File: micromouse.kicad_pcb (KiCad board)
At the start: 2 copper layers, 115.3 x 122.3 mm, 14 parts, among them J1 XT60-M, SW2 SW_Push, SW3 SW_SPDT_312, SW4 SW_Push, U1 BUCK, U2 STM32 Blackpill, U3 N20 encoder right, U4 N20 encoder left, U5 TB6612FNG, U6 VL53L0X left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

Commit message: pcb
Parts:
- SW2, SW4: footprint push button:push_button -> push button 1:SW_VS-1213-67-160GF
- moved U7 2.27 mm to (183.3, 50.1)
- moved SW4 1.72 mm to (129.1, 63.4)
- moved SW2 1.69 mm to (170.9, 63.3)
- moved U6 1.08 mm to (116.8, 67.8)
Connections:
- U5 pad 2: 5v -> 3.3v
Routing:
- net 3.3v: track 268.7 -> 324.7 mm
- net 5v: track 104.5 -> 83.3 mm
- net XSHUT 3: track 51.2 -> 53.9 mm
- net SCL: track 216.0 -> 218.2 mm
- net XSHUT 1: track 50.6 -> 51.9 mm
- net SDA: track 194.5 -> 193.7 mm
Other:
- board size 115.3 x 122.3 mm -> 115 x 122.4 mm

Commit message: pcb changes
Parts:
- added G***: LOGO, rnc:rnc3, F.Cu at (129.7, 49.1)
- added SW1: SW_SPST, power switch:battery_sw, F.Cu at (195.4, 131.8)
- moved U7 0.91 mm to (182.8, 49.4)
- moved U6 0.90 mm to (117.5, 67.2)
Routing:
- net 7.4vb: track 11.5 -> 38.3 mm
- net 7.4v: track 0.00 -> 15.0 mm
- net AIN1: track 45.7 -> 47.5 mm
- net XSHUT 1: track 51.9 -> 50.6 mm
- net BO2: track 30.1 -> 31.1 mm
- net XSHUT 3: track 53.9 -> 53.1 mm
- net AIN2: track 45.7 -> 46.5 mm
- net SDA: track 193.7 -> 193.1 mm
- net SCL: track 218.2 -> 218.8 mm
- added copper zone on B.Cu, net GND
- added copper zone on F.Cu, net GND
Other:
- outline, holes or cut-outs redrawn

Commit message: changes
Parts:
- moved U7 2.29 mm to (180.9, 48.1)
- moved U6 2.16 mm to (119.1, 65.8)
- moved U8 0.33 mm to (140.9, 44.2)
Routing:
- net SDA: track 193.1 -> 190.0 mm
- net XSHUT 3: track 53.1 -> 55.3 mm
- net GND: track 367.5 -> 366.2 mm
- net 3.3v: track 324.6 -> 323.3 mm
- net XSHUT 1: track 50.6 -> 51.3 mm

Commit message: final
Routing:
- net slide_SW: track 55.5 -> 86.6 mm, vias 1 -> 0
- net SCL: track 219.2 -> 189.6 mm
- net GND: track 366.2 -> 395.0 mm
- net XSHUT 3: track 55.3 -> 37.7 mm
- net STBY: track 88.6 -> 103.7 mm, vias 0 -> 1
- net 3.3v: track 323.3 -> 308.8 mm, vias 0 -> 1
- net XSHUT 1: track 51.3 -> 57.9 mm
- net BO1: track 67.9 -> 71.0 mm
- net XSHUT 2: track 54.5 -> 53.3 mm
- net AO1: track 24.8 -> 26.0 mm
- net push button: track 30.6 -> 31.5 mm
- net SDA: track 190.0 -> 189.3 mm
- net push button 1: track 57.9 -> 58.5 mm
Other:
- outline, holes or cut-outs redrawn

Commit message: hello world
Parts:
- removed G***: LOGO, rnc:rnc3
- removed U9: oled i2c, oled:oled
- ACC1: moved to B.Cu
- U6: value VL53L0X left -> VL6180X; footprint VL53L0X:VL53L0X -> VL6180X:VL6180X
- U7: value VL53L0X right -> VL6180X; footprint VL53L0X:VL53L0X -> VL6180X:VL6180X
- U8: value VL53L0X middle -> VL6180X; footprint VL53L0X:VL53L0X -> VL6180X:VL6180X
- moved SW2 279.7 mm to (-108.8, 65.7), turned to 0 degrees
- moved J1 263.0 mm to (-48.8, 53.1), turned to 90 degrees
- moved U2 257.7 mm to (-117.1, 100.6), turned to 0 degrees
- moved SW1 247.7 mm to (-49.3, 93.3), turned to -90 degrees
- moved SW3 235.7 mm to (405.8, 91.7)
- moved U1 230.4 mm to (-50.0, 77.0), turned to 180 degrees
- moved SW4 197.1 mm to (-68.0, 66.3), turned to 0 degrees
- moved U3 181.6 mm to (-12.2, 87.9)
- moved U4 146.6 mm to (-12.1, 58.9)
- moved U5 66.3 mm to (147.6, 73.4), turned to 90 degrees
- moved U6 54.0 mm to (171.5, 52.8), turned to -90 degrees
- moved U7 32.7 mm to (148.9, 55.0), turned to 0 degrees
- moved U8 18.1 mm to (124.1, 51.0), turned to 90 degrees
- moved ACC1 2.89 mm to (158.5, 71.9), turned to -90 degrees
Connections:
- U6 pad 1: 3.3v -> unconnected-(U6-GPIO1-Pad1)
- U6 pad 2: GND -> XSHUT 3
- U6 pad 5: unconnected-(U6-GPIO1-Pad5) -> 3.3v
- U6 pad 6: XSHUT 3 -> GND
- U7 pad 1: 3.3v -> unconnected-(U7-GPIO1-Pad1)
- U7 pad 2: GND -> XSHUT 1
- U7 pad 5: unconnected-(U7-GPIO1-Pad5) -> 3.3v
- U7 pad 6: XSHUT 1 -> GND
- U8 pad 1: 3.3v -> (no net)
- U8 pad 2: GND -> (no net)
- U8 pad 3: SCL -> (no net)
- U8 pad 4: SDA -> (no net)
- U8 pad 5: unconnected-(U8-GPIO1-Pad5) -> (no net)
- U8 pad 6: XSHUT 2 -> (no net)
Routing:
- net GND: track 395.0 -> 0.00 mm
- net 3.3v: track 308.8 -> 0.00 mm, vias 1 -> 0
- net SCL: track 189.6 -> 0.00 mm, vias 1 -> 0
- net SDA: track 189.3 -> 0.00 mm
- net STBY: track 103.7 -> 0.00 mm, vias 1 -> 0
- net slide_SW: track 86.6 -> 0.00 mm
- net 5v: track 83.3 -> 0.00 mm
- net BO1: track 71.0 -> 0.00 mm
- net push button 1: track 58.5 -> 0.00 mm, vias 2 -> 0
- net XSHUT 1: track 57.9 -> 0.00 mm
- net XSHUT 2: track 53.3 -> 0.00 mm
- net AIN1: track 47.5 -> 0.00 mm
- net AIN2: track 46.5 -> 0.00 mm
- net PWM A: track 45.7 -> 0.00 mm
- net BIN1: track 43.2 -> 0.00 mm
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- removed copper zone on B.Cu, net GND
- removed copper zone on F.Cu, net GND
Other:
- board size 115 x 122.4 mm -> 682 x 201.6 mm
- board text removed: "0.96 Inch I2C/IIC 4pin OLED Display"
- board text removed: "A01"
- board text removed: "AIN1"
- board text removed: "AIN2"
- board text removed: "AO2"
- board text removed: "B01"
- board text removed: "BIN1"
- board text removed: "BIN2"
- board text removed: "BO2"
- board text removed: "GY-53 VL53L0X"
- board text removed: "PWMA"
- board text removed: "PWMB"
- board text removed: "STBY"
- board text removed: "TB6612FNG"
- board text removed: "Vm"

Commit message: hello
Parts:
- U3: moved to B.Cu
- moved SW4 281.0 mm to (206.3, 127.0)
- moved U2 240.9 mm to (123.4, 113.8)
- moved SW2 214.6 mm to (98.1, 122.7)
- moved SW1 159.6 mm to (102.6, 142.3)
- moved U3 117.9 mm to (98.1, 129.4), turned to 0 degrees
- moved U4 7.14 mm to (-12.7, 66.0)
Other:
- board text removed: "5V"
- board text removed: "A0"
- board text removed: "A1"
- board text removed: "A10"
- board text removed: "A11"
- board text removed: "A12"
- board text removed: "A15"
- board text removed: "A2"
- board text removed: "A3"
- board text removed: "A4"
- board text removed: "A5"
- board text removed: "A6"
- board text removed: "A7"
- board text removed: "A8"
- board text removed: "A9"
- board text removed: "B0"
- board text removed: "B1"
- board text removed: "B10"
- board text removed: "B12"
- board text removed: "B13"
- board text removed: "B14"
- board text removed: "B15"
- board text removed: "B2"
- board text removed: "B3"
- board text removed: "B4"
- board text removed: "B5"
- board text removed: "B6"
- board text removed: "B7"
- board text removed: "B8"
- board text removed: "B9"
- board text removed: "BlackPill STM32F411CEU6 F411"
- board text removed: "C1"
- board text removed: "C13"
- board text removed: "C14"
- board text removed: "C15"
- board text removed: "C2"
- board text removed: "HW-290/GY-87 10DOF MPU6050"
- board text removed: "M1"
- board text removed: "M2"
- board text removed: "R"
- board text removed: "VB"
- board text removed: "Vcc"

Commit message: pcb
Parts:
- added REF**: n20 motor, n20 motor:n20 motor, F.Cu at (118.6, 100.1)
- added REF**: n20 motor, n20 motor:n20 motor, F.Cu at (149.6, 100.2)
- added REF**: n20 bracket, n20-bracket:Untitled, F.Cu at (152.4, 100.2)
- added REF**: n20 bracket, n20-bracket:Untitled, F.Cu at (115.8, 100.2)
- added REF**: castor, castor:castor, B.Cu at (134.2, 52.2)
- U3: moved to F.Cu
- U6, U7, U8: moved to B.Cu
- moved SW3 273.2 mm to (134.1, 120.2), turned to 0 degrees
- moved J1 216.4 mm to (166.6, 32.5)
- moved U1 173.0 mm to (117.3, 33.3), turned to 0 degrees
- moved U4 134.8 mm to (112.0, 117.1)
- moved SW1 108.6 mm to (102.6, 33.7), turned to 90 degrees
- moved SW2 104.7 mm to (152.7, 33.3), turned to 180 degrees
- moved SW4 71.1 mm to (176.0, 62.7), turned to 90 degrees
- moved U3 60.6 mm to (157.5, 117.3), turned to -90 degrees
- moved U2 51.9 mm to (113.0, 63.0)
- moved ACC1 36.5 mm to (123.2, 81.3), turned to 90 degrees
- moved U8 27.0 mm to (98.9, 41.4), turned to -90 degrees
- moved U7 23.6 mm to (134.1, 36.7), turned to 180 degrees
- moved U5 14.8 mm to (157.2, 62.2), turned to -90 degrees
- moved U6 11.7 mm to (169.3, 41.4), turned to 90 degrees
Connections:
- U8 pad 1: (no net) -> unconnected-(U8-GPIO1-Pad1)
- U8 pad 2: (no net) -> XSHUT 2
- U8 pad 3: (no net) -> SCL
- U8 pad 4: (no net) -> SDA
- U8 pad 5: (no net) -> 3.3v
- U8 pad 6: (no net) -> GND
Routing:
- net GND: track 0.00 -> 420.4 mm, vias 0 -> 4
- net 3.3v: track 0.00 -> 259.8 mm
- net SDA: track 0.00 -> 199.4 mm
- net SCL: track 0.00 -> 188.5 mm
- net 7.4vb: track 0.00 -> 95.6 mm
- net BO2: track 0.00 -> 93.8 mm
- net XSHUT 3: track 0.00 -> 92.3 mm, vias 0 -> 1
- net BO1: track 0.00 -> 87.8 mm
- net push button: track 0.00 -> 81.1 mm, vias 0 -> 1
- net XSHUT 1: track 0.00 -> 80.1 mm
- net 7.4v: track 0.00 -> 77.0 mm
- net STBY: track 0.00 -> 75.9 mm
- net AO1: track 0.00 -> 74.1 mm
- net encoder B2: track 0.00 -> 74.1 mm
- net encoder A2: track 0.00 -> 71.3 mm
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- added copper zone on B.Cu, net GND
- added copper zone on F.Cu, net GND
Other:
- board size 682 x 201.6 mm -> 98.1 x 98.9 mm
- board text removed: "+"
- board text removed: "+ve"
- board text removed: "3.3v"
- board text removed: "5v"
- board text removed: "7.4v"
- board text removed: "DC-DC 5V 3A BEC Power Supply Buck Step Down Module"
- board text removed: "GA12-N20-6v 500 RPM"
- board text removed: "GND"
- board text removed: "GPIO1"
- board text removed: "MCU"
- board text removed: "SCL"
- board text removed: "SDA"
- board text removed: "Slide Switch SS-12D00 1P2T"
- board text removed: "Tactile Push Button"
- board text removed: "XSHUT"
- board text removed: "XT-60"

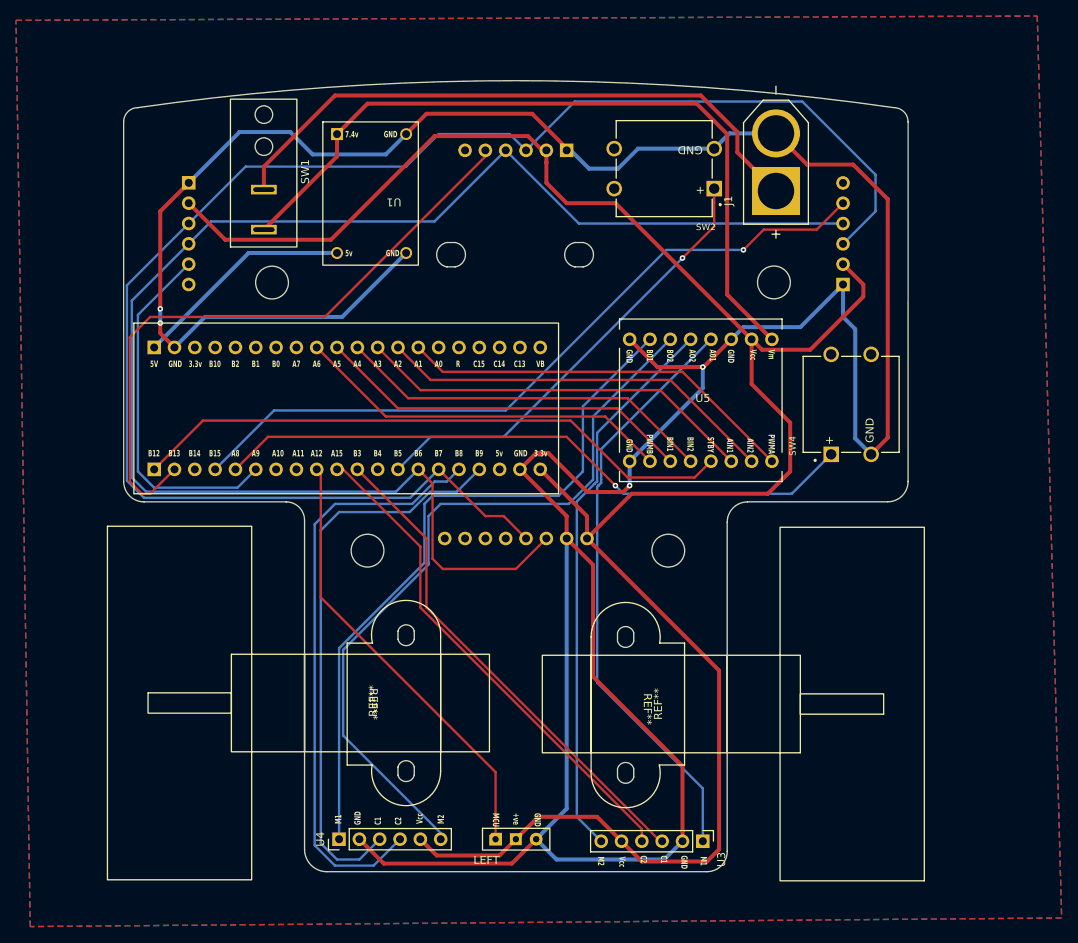
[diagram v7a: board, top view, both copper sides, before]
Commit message: added uart
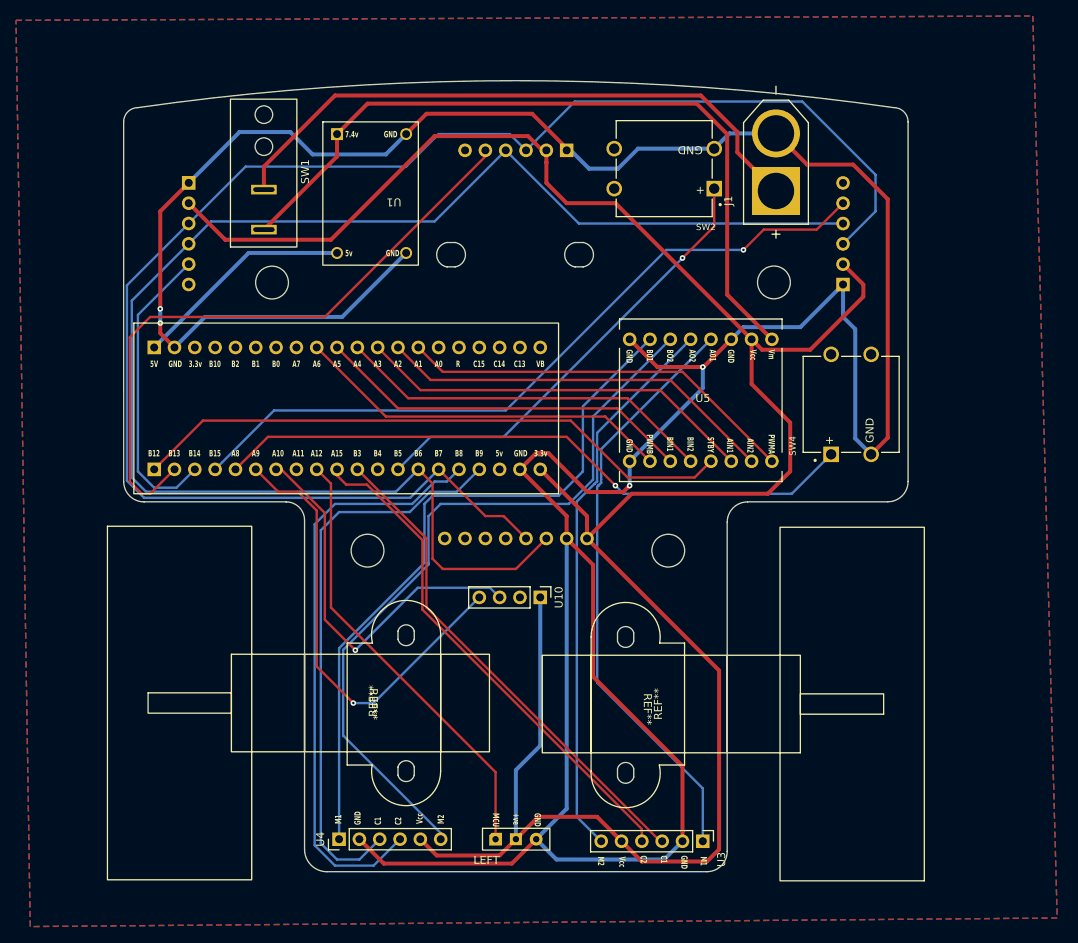
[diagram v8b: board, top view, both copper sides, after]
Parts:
- added U10: UART, Connector_PinHeader_2.54mm:PinHeader_1x04_P2.54mm_Vertical, F.Cu at (137.2, 86.9)
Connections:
- U2 pad 3: unconnected-(U2-B14-Pad3) -> XSHUT 2
- U2 pad 6: XSHUT 2 -> Tx
- U2 pad 7: unconnected-(U2-A10-Pad7) -> Rx
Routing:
- net Tx: track 0.00 -> 56.9 mm, vias 0 -> 1
- net Rx: track 0.00 -> 48.8 mm, vias 0 -> 1
- net 3.3v: track 259.8 -> 291.3 mm
- net XSHUT 2: track 45.1 -> 37.4 mm
- net encoder B1: track 62.7 -> 63.8 mm
